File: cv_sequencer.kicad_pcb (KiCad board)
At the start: 4 copper layers, 108.7 x 22.4 mm, 36 parts, among them J1 3085_MiniJack_Thonk_Vert, J10 3096_USBC_RA_SMD, J11 4005_SWD_Header, J2 3085_MiniJack_Thonk_Vert, J3 3085_MiniJack_Thonk_Vert, J4 3085_MiniJack_Thonk_Vert, J5 3085_MiniJack_Thonk_Vert, J6 3085_MiniJack_Thonk_Vert, J7 3085_MiniJack_Thonk_Vert, J8 3085_MiniJack_Thonk_Vert, J9 3086_Connector_Eurorack_Power, U1 3097_TFT_Display_SPI, U2 3093_MIC5225_3v3, U3 4002_RP2040, U4 4001_MCP48FEB24_DAC, Y1 4004-Crystal-12MHz_GND24

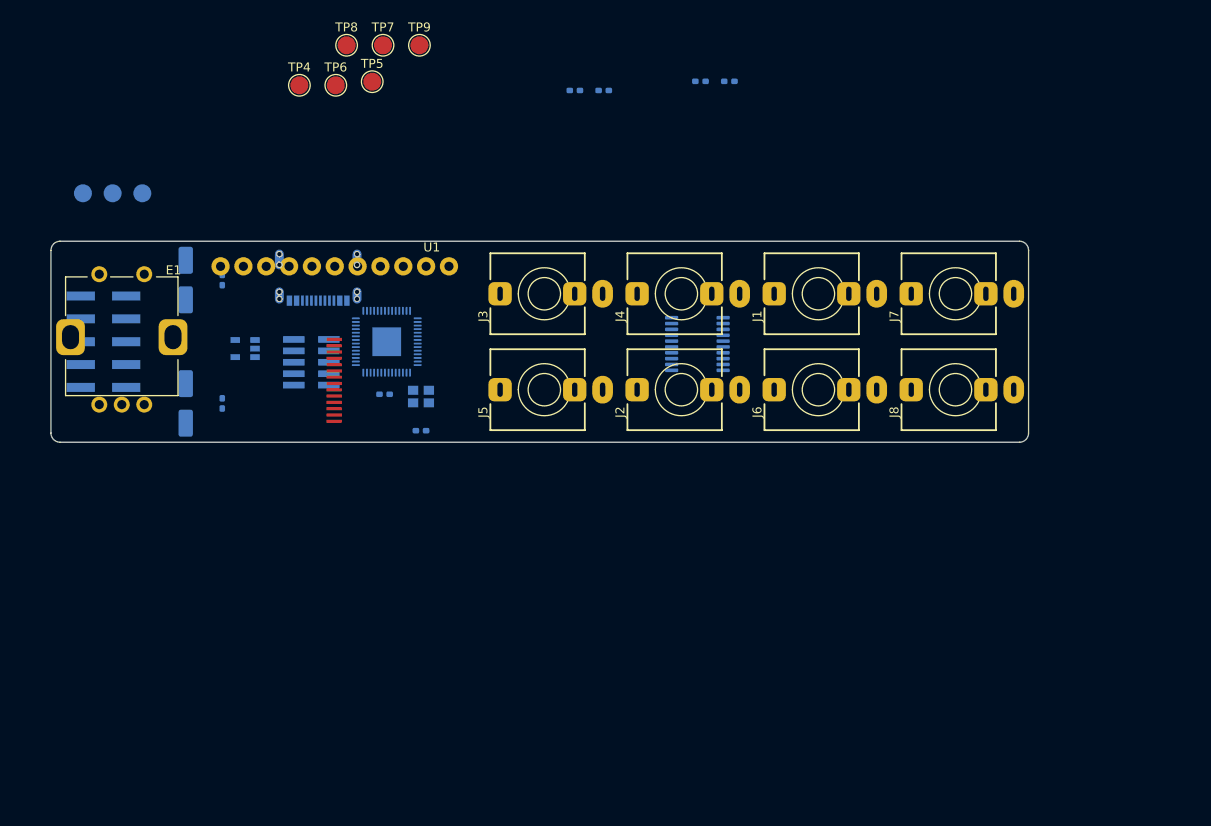
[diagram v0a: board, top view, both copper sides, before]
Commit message: ran ERC, minimal errors. Imported footprints and started grouping them
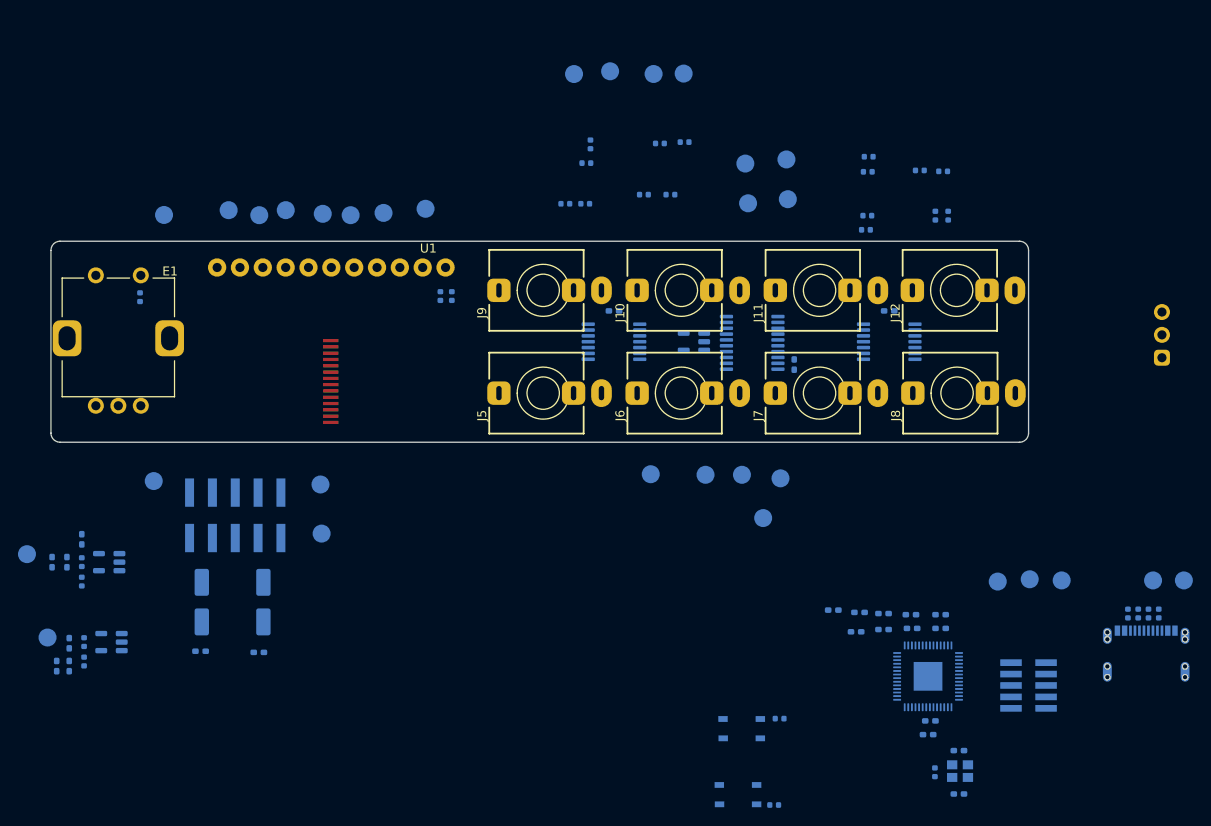
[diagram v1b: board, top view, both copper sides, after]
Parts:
- added C11: 3089_Capacitor_100n_16V_0402, Shulltronics_Generics:C_0402_HandSolder, B.Cu at (205.6, 106.0)
- added C12: 3089_Capacitor_100n_16V_0402, Shulltronics_Generics:C_0402_HandSolder, B.Cu at (204.5, 117.9)
- added C13: 3089_Capacitor_100n_16V_0402, Shulltronics_Generics:C_0402_HandSolder, B.Cu at (108.7, 111.8)
- added C14: 3089_Capacitor_100n_16V_0402, Shulltronics_Generics:C_0402_HandSolder, B.Cu at (204.2, 119.4)
- added C15: 4013_Capacitor_1u_16V_0402, Shulltronics_Generics:C_0402_HandSolder, B.Cu at (108.7, 109.2)
- added C16: 3089_Capacitor_100n_16V_0402, Shulltronics_Generics:C_0402_HandSolder, B.Cu at (106.8, 100.2)
- added C17: 4013_Capacitor_1u_16V_0402, Shulltronics_Generics:C_0402_HandSolder, B.Cu at (108.5, 100.2)
- added C18: 4013_Capacitor_1u_16V_0402, Shulltronics_Generics:C_0402_HandSolder, B.Cu at (110.1, 97.7)
- added C19: 4013_Capacitor_1u_16V_0402, Shulltronics_Generics:C_0402_HandSolder, B.Cu at (107.3, 111.8)
- added C20: 3089_Capacitor_100n_16V_0402, Shulltronics_Generics:C_0402_HandSolder, B.Cu at (123.3, 110.1)
- added C21: 3089_Capacitor_100n_16V_0402, Shulltronics_Generics:C_0402_HandSolder, B.Cu at (129.8, 110.2)
- added C22: 3088_Capacitor_10u_50V_SMD, Shulltronics_Passives:3088_Capacitor_10u_50V_SMD, B.Cu at (123.5, 104.6)
- added C23: 3088_Capacitor_10u_50V_SMD, Shulltronics_Passives:3088_Capacitor_10u_50V_SMD, B.Cu at (130.3, 104.6)
- added C24: 3089_Capacitor_100n_16V_SMD, Shulltronics_Generics:C_0402_HandSolder, B.Cu at (189.3, 78.2)
- added C25: 3089_Capacitor_100n_16V_SMD, Shulltronics_Generics:C_0402_HandSolder, B.Cu at (169.3, 72.3)
- added C26: 3089_Capacitor_100n_16V_SMD, Shulltronics_Generics:C_0402_HandSolder, B.Cu at (199.9, 72.3)
- added J12: 3085_MiniJack_Thonk_Vert, Shulltronics_Connectors:3085_MiniJack_Thonk_Vert, F.Cu at (207.4, 70.0)
- added R1: 4008_Resistor_SMD_10k_0.125W_1%, Shulltronics_Generics:RES-0402, B.Cu at (116.6, 70.7)
- added R10: 4020_Resistor_SMD_180k_0.125W_1%, Shulltronics_Generics:RES-0402, B.Cu at (110.4, 111.3)
- added R11: 4019_Resistor_SMD_270k_0.125W_1%, Shulltronics_Generics:RES-0402, B.Cu at (110.1, 100.2)
- added R12: 4018_Resistor_SMD_82k_0.125W_1%, Shulltronics_Generics:RES-0402, B.Cu at (110.1, 102.4)
- added R13: 4009_Resistor_SMD_5k1_0.10W_1%, Shulltronics_Generics:RES-0402, B.Cu at (229.9, 105.9)
- added R14: 4009_Resistor_SMD_5k1_0.10W_1%, Shulltronics_Generics:RES-0402, B.Cu at (226.4, 105.9)
- added R15: 4023_Resistor_SMD_56k_0.125W_1%, Shulltronics_Generics:RES-0402, B.Cu at (175.6, 59.3)
- added R16: 4023_Resistor_SMD_56k_0.125W_1%, Shulltronics_Generics:RES-0402, B.Cu at (177.1, 53.5)
- added R17: 4023_Resistor_SMD_56k_0.125W_1%, Shulltronics_Generics:RES-0402, B.Cu at (166.2, 55.8)
- added R18: 4023_Resistor_SMD_56k_0.125W_1%, Shulltronics_Generics:RES-0402, B.Cu at (166.1, 60.4)
- added R19: 4022_Resistor_SMD_120k_0.125W_1%, Shulltronics_Generics:RES-0402, B.Cu at (172.6, 59.3)
- added R2: DNP, Shulltronics_Generics:RES-0402, B.Cu at (150.0, 70.6)
- added R20: 4022_Resistor_SMD_120k_0.125W_1%, Shulltronics_Generics:RES-0402, B.Cu at (174.4, 53.6)
- added R21: 4022_Resistor_SMD_120k_0.125W_1%, Shulltronics_Generics:RES-0402, B.Cu at (166.7, 53.7)
- added R22: 4022_Resistor_SMD_120k_0.125W_1%, Shulltronics_Generics:RES-0402, B.Cu at (163.9, 60.4)
- added R23: 4006_Resistor_SMD_68k_0.125W_1%, Shulltronics_Generics:RES-0402, B.Cu at (205.0, 61.7)
- added R24: 4006_Resistor_SMD_68k_0.125W_1%, Shulltronics_Generics:RES-0402, B.Cu at (205.9, 56.7)
- added R25: 4006_Resistor_SMD_68k_0.125W_1%, Shulltronics_Generics:RES-0402, B.Cu at (197.5, 56.8)
- added R26: 4006_Resistor_SMD_68k_0.125W_1%, Shulltronics_Generics:RES-0402, B.Cu at (197.3, 63.2)
- added R27: 4006_Resistor_SMD_68k_0.125W_1%, Shulltronics_Generics:RES-0402, B.Cu at (206.5, 61.7)
- added R28: 4006_Resistor_SMD_68k_0.125W_1%, Shulltronics_Generics:RES-0402, B.Cu at (203.3, 56.6)
- added R29: 4006_Resistor_SMD_68k_0.125W_1%, Shulltronics_Generics:RES-0402, B.Cu at (197.6, 55.1)
- added R3: 4021_Resistor_SMD_Jumper, Shulltronics_Generics:RES-0402, B.Cu at (151.3, 70.6)
- added R30: 4006_Resistor_SMD_68k_0.125W_1%, Shulltronics_Generics:RES-0402, B.Cu at (197.5, 61.7)
- added R4: 4010_Resistor_SMD_1k_0.125W_1%, Shulltronics_Generics:RES-0402, B.Cu at (205.0, 123.6)
- added R5: 4010_Resistor_SMD_1k_0.125W_1%, Shulltronics_Generics:RES-0402, B.Cu at (187.1, 127.2)
- added R6: 4011_Resistor_SMD_27_0.125W_1%, Shulltronics_Generics:RES-0402, B.Cu at (228.7, 105.9)
- added R7: 4011_Resistor_SMD_27_0.125W_1%, Shulltronics_Generics:RES-0402, B.Cu at (227.6, 105.9)
- added R8: 4008_Resistor_SMD_10k_0.125W_1%, Shulltronics_Generics:RES-0402, B.Cu at (187.7, 117.6)
- added R9: 4019_Resistor_SMD_270k_0.125W_1%, Shulltronics_Generics:RES-0402, B.Cu at (110.4, 109.1)
- added SW1: RST, Shulltronics_ElectroMechanical:4012_PushButton_NO_SMD, B.Cu at (183.5, 118.6)
- added SW2: BOOTSEL, Shulltronics_ElectroMechanical:4012_PushButton_NO_SMD, B.Cu at (183.1, 126.0)
- added TP10: 5V3, Shulltronics_Generics:TestPoint_Pad_D2.0mm, B.Cu at (104.0, 99.3)
- added TP11: USB_D-, Shulltronics_Generics:TestPoint_Pad_D2.0mm, B.Cu at (232.7, 102.2)
- added TP12: USB_D+, Shulltronics_Generics:TestPoint_Pad_D2.0mm, B.Cu at (229.2, 102.2)
- added TP13: +12V, Shulltronics_Generics:TestPoint_Pad_D2.0mm, B.Cu at (118.1, 91.2)
- added TP14: -12V, Shulltronics_Generics:TestPoint_Pad_D2.0mm, B.Cu at (136.7, 91.6)
- added TP15: SWDIO, Shulltronics_Generics:TestPoint_Pad_D2.0mm, B.Cu at (219.1, 102.2)
- added TP16: SWCLK, Shulltronics_Generics:TestPoint_Pad_D2.0mm, B.Cu at (215.5, 102.1)
- added TP17: GND, Shulltronics_Generics:TestPoint_Pad_D2.0mm, B.Cu at (136.8, 97.0)
- added TP18: ~{RST}, Shulltronics_Generics:TestPoint_Pad_D2.0mm, B.Cu at (212.0, 102.4)
- added TP19: DAC_SDI, Shulltronics_Generics:TestPoint_Pad_D2.0mm, B.Cu at (187.8, 90.9)
- added TP20: DAC_SCK, Shulltronics_Generics:TestPoint_Pad_D2.0mm, B.Cu at (185.9, 95.3)
- added TP21: DAC_VOUT0, Shulltronics_Generics:TestPoint_Pad_D2.0mm, B.Cu at (188.6, 59.8)
- added TP22: DAC_SDO, Shulltronics_Generics:TestPoint_Pad_D2.0mm, B.Cu at (179.5, 90.5)
- added TP23: DAC_~{CS}, Shulltronics_Generics:TestPoint_Pad_D2.0mm, B.Cu at (183.5, 90.5)
- added TP24: DAC_VOUT1, Shulltronics_Generics:TestPoint_Pad_D2.0mm, B.Cu at (183.9, 55.9)
- added TP25: DAC_VOUT2, Shulltronics_Generics:TestPoint_Pad_D2.0mm, B.Cu at (188.5, 55.4)
- added TP26: DAC_VOUT3, Shulltronics_Generics:TestPoint_Pad_D2.0mm, B.Cu at (184.2, 60.3)
- added TP27: VREF_5V0, Shulltronics_Generics:TestPoint_Pad_D2.0mm, B.Cu at (173.4, 90.4)
- added TP28: TRIG0, Shulltronics_Generics:TestPoint_Pad_D2.0mm, B.Cu at (177.0, 45.9)
- added TP29: TRIG1, Shulltronics_Generics:TestPoint_Pad_D2.0mm, B.Cu at (173.7, 45.9)
- added TP30: TRIG2, Shulltronics_Generics:TestPoint_Pad_D2.0mm, B.Cu at (168.9, 45.6)
- added TP31: TRIG3, Shulltronics_Generics:TestPoint_Pad_D2.0mm, B.Cu at (164.8, 45.9)
- added U5: 4014_Voltage_Reference_5V_SOT23-6, Shulltronics_Generics:SOT-23-5, B.Cu at (178.2, 75.7)
- added U6: 4001_MCP48FEB24_DAC, Shulltronics_Generics:TSSOP-20_4.4x6.5mm_P0.65mm, B.Cu at (184.7, 75.8)
- added U7: 3099_TL074CPW_SMD, Shulltronics_Integrated_Circuits:3099_TL074CPW_TSSOP14, B.Cu at (169.3, 75.7)
- added U8: 3099_TL074CPW_SMD, Shulltronics_Integrated_Circuits:3099_TL074CPW_TSSOP14, B.Cu at (199.9, 75.7)
- C1, C2: value 3088_Capacitor_10u_50V_SMD -> 3089_Capacitor_100n_16V_0402; footprint Shulltronics_Passives:3088_Capacitor_10u_50V_SMD -> Shulltronics_Generics:C_0402_HandSolder
- C3, C4, C5, C6, C7: value 3089_Capacitor_100n_16V_SMD -> 3089_Capacitor_100n_16V_0402
- C8: value 3089_Capacitor_100n_16V_SMD -> 4003_Capacitor_22pF_50V_0402
- C9: value 4003_Capacitor_22pF_50V_0402 -> 3089_Capacitor_100n_16V_0402
- J1: value 3085_MiniJack_Thonk_Vert -> 4005_SWD_Header; footprint Shulltronics_Connectors:3085_MiniJack_Thonk_Vert -> Shulltronics_Connectors:4005_SWD_Header; moved to B.Cu
- J10: value 3096_USBC_RA_SMD -> 3085_MiniJack_Thonk_Vert; footprint Shulltronics_Connectors:3096_USBC_RA -> Shulltronics_Connectors:3085_MiniJack_Thonk_Vert; moved to F.Cu
- J11: value 4005_SWD_Header -> 3085_MiniJack_Thonk_Vert; footprint Shulltronics_Connectors:4005_SWD_Header -> Shulltronics_Connectors:3085_MiniJack_Thonk_Vert; moved to F.Cu
- J2: value 3085_MiniJack_Thonk_Vert -> 3086_Connector_Eurorack_Power; footprint Shulltronics_Connectors:3085_MiniJack_Thonk_Vert -> Shulltronics_Connectors:3086_SMD_Eurorack_Power; moved to B.Cu
- J3: value 3085_MiniJack_Thonk_Vert -> 3096_USBC_RA_SMD; footprint Shulltronics_Connectors:3085_MiniJack_Thonk_Vert -> Shulltronics_Connectors:3096_USBC_RA; moved to B.Cu
- J4: value 3085_MiniJack_Thonk_Vert -> CV_OFFSET; footprint Shulltronics_Connectors:3085_MiniJack_Thonk_Vert -> Shulltronics_Connectors:3046_Header_3pos_2.54mm; moved to B.Cu
- J9: value 3086_Connector_Eurorack_Power -> 3085_MiniJack_Thonk_Vert; footprint Shulltronics_Connectors:3086_SMD_Eurorack_Power -> Shulltronics_Connectors:3085_MiniJack_Thonk_Vert; moved to F.Cu
- TP1: value +12V -> ENC_BTN
- TP2: value -12V -> LCD/SD_SCK
- TP3: value GND -> SD_SDO
- TP4: value TestPoint -> LCD/SD_SDI; moved to B.Cu
- TP5: value TestPoint -> LCD_CS; moved to B.Cu
- TP6: value TestPoint -> LCD_RST; moved to B.Cu
- TP7: value TestPoint -> LCD_DC; moved to B.Cu
- TP8: value TestPoint -> SD_CS; moved to B.Cu
- TP9: value TestPoint -> 3V1; moved to B.Cu
- U2: value 3093_MIC5225_3v3 -> 4002_RP2040; footprint Shulltronics_Regulators:3093_MIC5225_3v3_LDO -> Shulltronics_Microcontrollers:4002_RP2040_QFN-56-7x7mm_P0.4mm
- U3: value 4002_RP2040 -> 4015_Adjustable_Reg_500mA_SOT-23-5; footprint Shulltronics_Microcontrollers:4002_RP2040_QFN-56-7x7mm_P0.4mm -> Shulltronics_Generics:SOT-23-5
- U4: value 4001_MCP48FEB24_DAC -> 4015_Adjustable_Reg_500mA_SOT-23-5; footprint Shulltronics_Generics:TSSOP-20_4.4x6.5mm_P0.65mm -> Shulltronics_Generics:SOT-23-5
- moved C1 92.5 mm to (205.6, 107.6), turned to 180 degrees
- moved C8 87.6 mm to (207.6, 126.0)
- moved U2 84.2 mm to (204.2, 112.9)
- moved C2 84.0 mm to (202.3, 106.0), turned to 180 degrees
- moved C3 82.4 mm to (199.3, 105.9), turned to 0 degrees
- moved C4 80.7 mm to (202.4, 107.6), turned to 180 degrees
- moved J3 78.4 mm to (228.5, 111.1), turned to 180 degrees
- moved TP9 77.8 mm to (106.3, 108.6), turned to 180 degrees
- moved C10 75.2 mm to (207.6, 121.2)
- moved Y1 73.0 mm to (207.8, 123.4), turned to 180 degrees
- moved U4 69.8 mm to (113.2, 100.2)
- moved C6 66.1 mm to (196.6, 105.8), turned to 180 degrees
- moved C5 64.3 mm to (199.3, 107.7), turned to 180 degrees
- moved C7 62.8 mm to (196.2, 108.0), turned to 180 degrees
- moved J11 57.1 mm to (192.2, 70.0), turned to 90 degrees
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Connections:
- C1 pad 1: VCC -> GND
- C1 pad 2: GND -> VCC
- C10 pad 1: unconnected-(C10-Pad1) -> GND
- C10 pad 2: unconnected-(C10-Pad2) -> /XOUT
- C2 pad 2: VSS -> VCC
- C3 pad 1: VCC -> GND
- C3 pad 2: GND -> VCC
- C4 pad 2: VSS -> VCC
- C5 pad 2: Net-(C5-Pad2) -> VCC
- C6 pad 1: unconnected-(C6-Pad1) -> GND
- C6 pad 2: unconnected-(C6-Pad2) -> VCC
- C7 pad 1: unconnected-(C7-Pad1) -> GND
- C7 pad 2: unconnected-(C7-Pad2) -> VCC
- C8 pad 1: unconnected-(C8-Pad1) -> GND
- C8 pad 2: unconnected-(C8-Pad2) -> /XIN
- C9 pad 1: unconnected-(C9-Pad1) -> GND
- C9 pad 2: unconnected-(C9-Pad2) -> VCC
- E1 pad 1: unconnected-(E1-Pad1) -> /ENC_1
- E1 pad 2: unconnected-(E1-Pad2) -> GND
- E1 pad 3: unconnected-(E1-Pad3) -> /ENC_0
- E1 pad 4: unconnected-(E1-Pad4) -> VCC
- E1 pad 5: unconnected-(E1-Pad5) -> /ENC_BTN
- J5 pad S: unconnected-(J5-PadS) -> GND
- J5 pad T: unconnected-(J5-PadT) -> Net-(J5-PadT)
- J6 pad S: unconnected-(J6-PadS) -> GND
- J6 pad T: unconnected-(J6-PadT) -> Net-(J6-PadT)
- J7 pad S: unconnected-(J7-PadS) -> GND
- J7 pad T: unconnected-(J7-PadT) -> Net-(J7-PadT)
- J8 pad S: unconnected-(J8-PadS) -> GND
- J8 pad T: unconnected-(J8-PadT) -> Net-(J8-PadT)
- TP1 pad 1: VCC -> /ENC_BTN
- TP2 pad 1: VSS -> /LCD/SD_SCK
- TP3 pad 1: GND -> /SD_SDO
- TP4 pad 1: unconnected-(TP4-Pad1) -> /LCD/SD_SDI
- TP5 pad 1: unconnected-(TP5-Pad1) -> /LCD_CS
- TP6 pad 1: unconnected-(TP6-Pad1) -> /LCD_RST
- TP7 pad 1: unconnected-(TP7-Pad1) -> /LCD_DC
- TP8 pad 1: unconnected-(TP8-Pad1) -> /SD_CS
- TP9 pad 1: unconnected-(TP9-Pad1) -> VCC
- U1 pad 1: unconnected-(U1-Pad1) -> /LCD_VIN
- U1 pad 10: unconnected-(U1-Pad10) -> /SD_CS
- U1 pad 3: unconnected-(U1-Pad3) -> GND
- U1 pad 4: unconnected-(U1-Pad4) -> /LCD/SD_SCK
- U1 pad 5: unconnected-(U1-Pad5) -> /SD_SDO
- U1 pad 6: unconnected-(U1-Pad6) -> /LCD/SD_SDI
- U1 pad 7: unconnected-(U1-Pad7) -> /LCD_CS
- U1 pad 8: unconnected-(U1-Pad8) -> /LCD_RST
- U1 pad 9: unconnected-(U1-Pad9) -> /LCD_DC
- U2 pad 2: GND -> /UART_TX
- U2 pad 3: unconnected-(U2-Pad3) -> /UART_RX
- U2 pad 4: unconnected-(U2-Pad4) -> /I2C_SDA
- U2 pad 5: Net-(C5-Pad2) -> /I2C_SCL
- U3 pad 1: unconnected-(U3-Pad1) -> VDD
- U3 pad 2: unconnected-(U3-Pad2) -> GND
- U3 pad 3: unconnected-(U3-Pad3) -> VDD
- U3 pad 4: unconnected-(U3-Pad4) -> Net-(R10-Pad2)
- U3 pad 5: unconnected-(U3-Pad5) -> VCC
- U4 pad 1: unconnected-(U4-Pad1) -> VDD
- U4 pad 2: unconnected-(U4-Pad2) -> GND
- U4 pad 3: unconnected-(U4-Pad3) -> VDD
- U4 pad 4: unconnected-(U4-Pad4) -> Net-(R11-Pad1)
- U4 pad 5: unconnected-(U4-Pad5) -> /5V3
- Y1 pad 1: unconnected-(Y1-Pad1) -> /XIN
- Y1 pad 2: unconnected-(Y1-Pad2) -> GND
- Y1 pad 3: unconnected-(Y1-Pad3) -> /XOUT
- Y1 pad 4: unconnected-(Y1-Pad4) -> GND

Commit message: more work on pcb, added some TODO notes to schematic
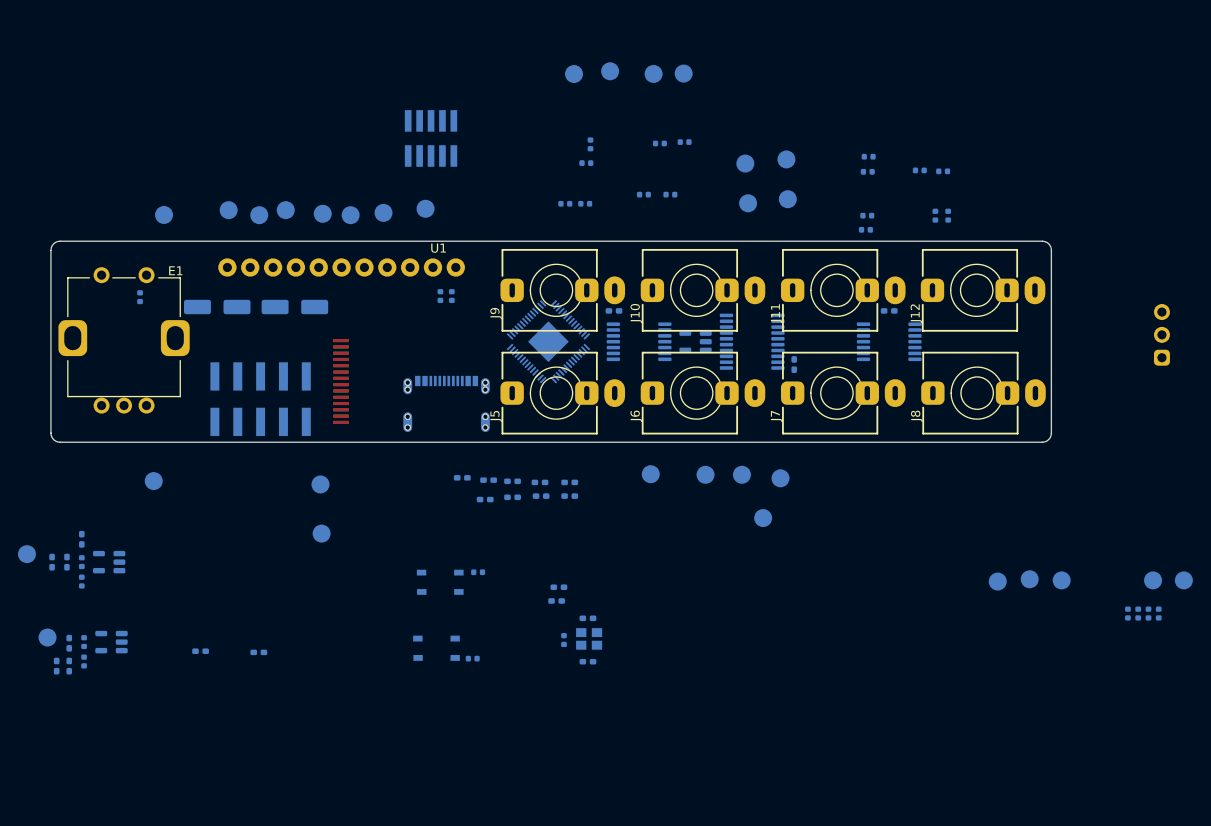
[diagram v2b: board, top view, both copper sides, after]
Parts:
- moved J1 90.1 mm to (148.9, 53.1), turned to -90 degrees
- moved J3 82.6 mm to (150.7, 83.4)
- moved U2 56.3 mm to (162.0, 75.7), turned to 45 degrees
- moved C12 43.9 mm to (163.2, 103.0)
- moved C14 43.9 mm to (162.9, 104.5)
- moved C2 43.8 mm to (161.1, 91.3)
- moved C3 43.8 mm to (158.0, 91.2)
- moved C7 43.8 mm to (155.0, 93.2)
- moved C9 43.8 mm to (152.4, 90.8)
- moved C10 43.8 mm to (166.4, 106.5)
- moved C5 43.8 mm to (158.0, 93.0)
- moved C6 43.8 mm to (155.3, 91.1)
- moved C8 43.8 mm to (166.4, 111.3)
- moved R4 43.8 mm to (163.7, 108.9)
- moved C1 43.8 mm to (164.4, 92.9)
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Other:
- board size 108.7 x 22.4 mm -> 111.3 x 22.4 mm
- board text added: "CV Sequencer Eurorack Module 1U, 22HP"
- board text removed: "CV Sequencer Eurorack Module 1U, 20HP"

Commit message: Changed encoder to SMD version
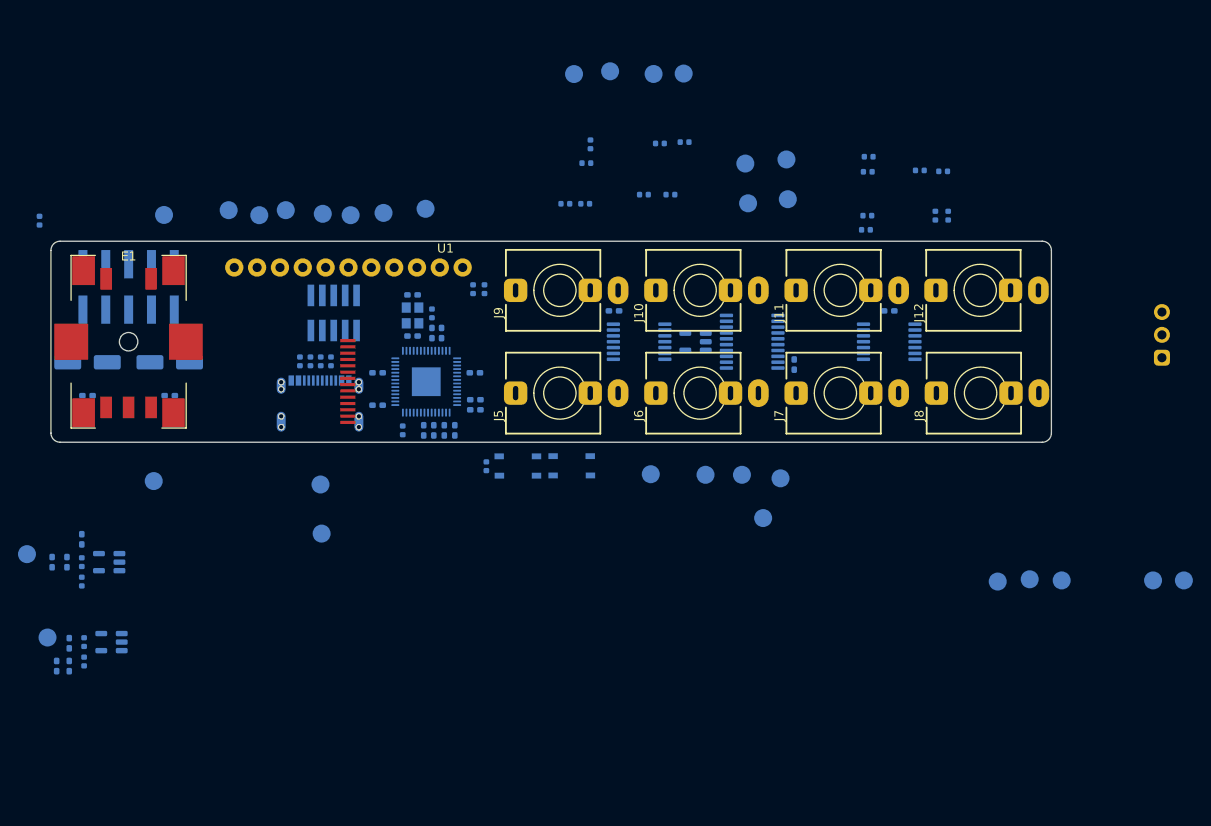
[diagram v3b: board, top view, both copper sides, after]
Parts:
- E1: value 3094_Encoder_Switch -> 4025_Encoder_Switch_SMD; footprint Shulltronics_ElectroMechanical:3094_Encoder_PEC11R -> Shulltronics_ElectroMechanical:4025_Encoder_PEC11S
- moved R14 96.3 mm to (134.4, 77.9)
- moved R13 96.2 mm to (137.8, 77.9)
- moved R6 96.2 mm to (136.7, 77.9), turned to 90 degrees
- moved R7 96.2 mm to (135.5, 77.9), turned to 90 degrees
- moved C8 41.1 mm to (146.9, 75.1)
- moved Y1 41.0 mm to (146.9, 72.8), turned to 90 degrees
- moved C10 40.9 mm to (146.9, 70.5), turned to 0 degrees
- moved R4 39.2 mm to (149.0, 72.5), turned to -90 degrees
- moved C12 31.1 mm to (150.1, 74.7), turned to 90 degrees
- moved C20 31.1 mm to (110.7, 81.7)
- moved C21 30.2 mm to (119.9, 81.7)
- moved R5 26.6 mm to (145.8, 85.5), turned to -90 degrees
- moved SW2 25.1 mm to (164.5, 89.6), turned to 0 degrees
- moved C11 23.0 mm to (143.0, 82.8), turned to 0 degrees
- moved C14 22.7 mm to (150.4, 85.5), turned to -90 degrees
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
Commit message: gots most components placed nicely, added 4027 for MIDI, still to finish
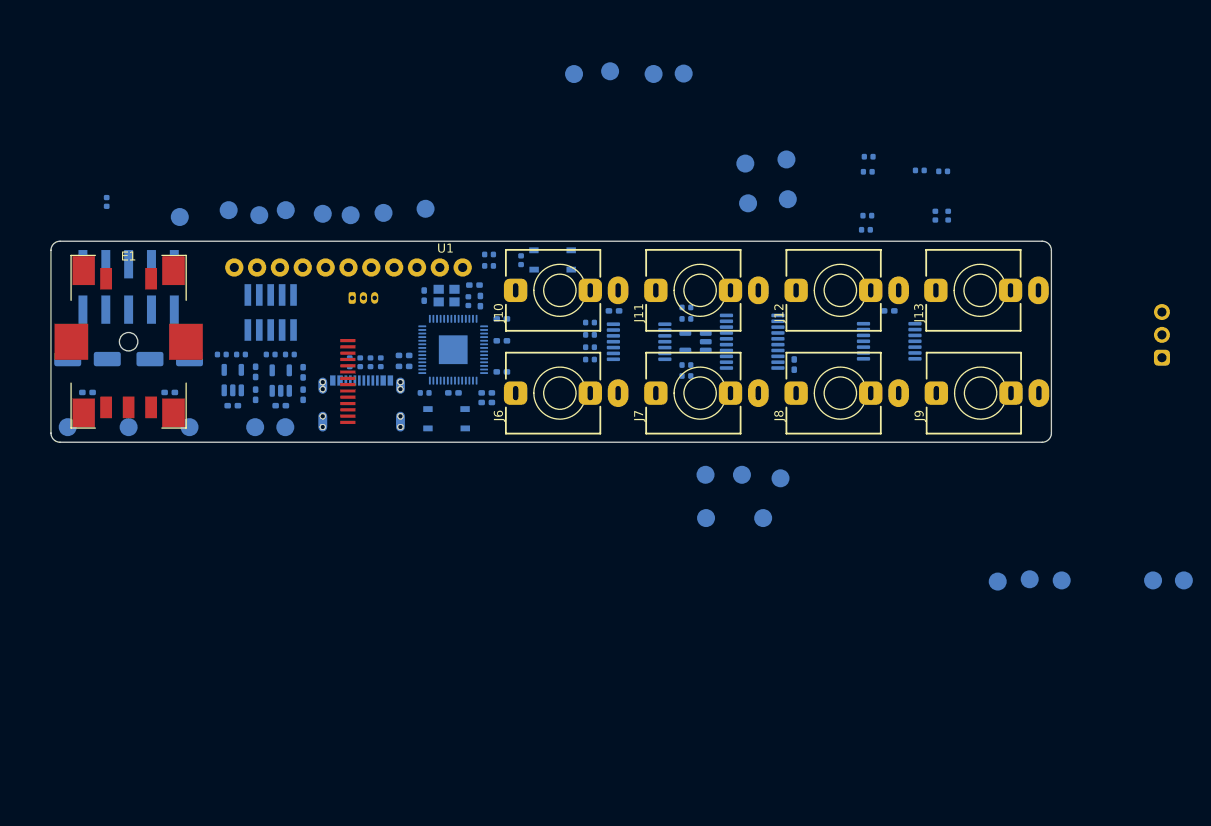
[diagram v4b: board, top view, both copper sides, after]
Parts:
- removed the C2 at (148.1, 85.5)
- removed the C3 at (153.9, 82.1)
- added J1: 4027_Connector_PicoBlade_3pos_Vert_THT, Shulltronics_Connectors:4027_PicoBlade_3pos_Vert_THT, B.Cu at (140.2, 70.8)
- moved R10 40.0 mm to (131.1, 77.1), turned to 0 degrees
- moved C11 39.8 mm to (134.7, 81.6)
- moved C13 39.8 mm to (134.7, 79.1), turned to -90 degrees
- moved R9 39.3 mm to (133.2, 77.1), turned to 0 degrees
- moved C17 38.2 mm to (132.2, 82.8), turned to 0 degrees
- moved TP9 35.3 mm to (132.7, 85.2)
- moved U3 34.6 mm to (132.2, 80.0), turned to 90 degrees
- moved C14 31.0 mm to (129.4, 79.0), turned to -90 degrees
- moved R12 29.7 mm to (125.7, 77.1), turned to 0 degrees
- moved R11 29.1 mm to (127.8, 77.1), turned to 0 degrees
- moved TP10 29.0 mm to (129.4, 85.2)
- moved C15 28.1 mm to (129.4, 81.6)
- moved TP17 24.5 mm to (115.3, 85.2)
- moved U4 24.5 mm to (126.9, 80.0), turned to 90 degrees
- moved R16 23.9 mm to (166.6, 74.9), turned to 0 degrees
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- renumbered C12 to C10, C13 to C11, C14 to C12, C15 to C13, C16 to C14, C17 to C15, C18 to C16, C19 to C17, C20 to C18, C21 to C19, C4 to C2, C22 to C20, C23 to C21, C24 to C22, C26 to C23, C25 to C24, C5 to C3, C6 to C4, C7 to C5, C8 to C6, C9 to C7, C10 to C8, C11 to C9, J9 to J10, J10 to J11, J11 to J12, J12 to J13, J1 to J2, J2 to J3, J3 to J4, J4 to J5, J5 to J6, J6 to J7, J7 to J8, J8 to J9, U8 to U7, U7 to U8
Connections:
- net Net-(J5-PadT) renamed /IO Jacks/TRIG0
- net Net-(J6-PadT) renamed /IO Jacks/TRIG1
- net Net-(J7-PadT) renamed /IO Jacks/TRIG2
- net Net-(J8-PadT) renamed /IO Jacks/TRIG3
